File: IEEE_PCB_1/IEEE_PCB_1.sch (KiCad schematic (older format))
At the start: 17 parts, among them U1 555, U2 4017, U3 EG1218, U4 1058TR

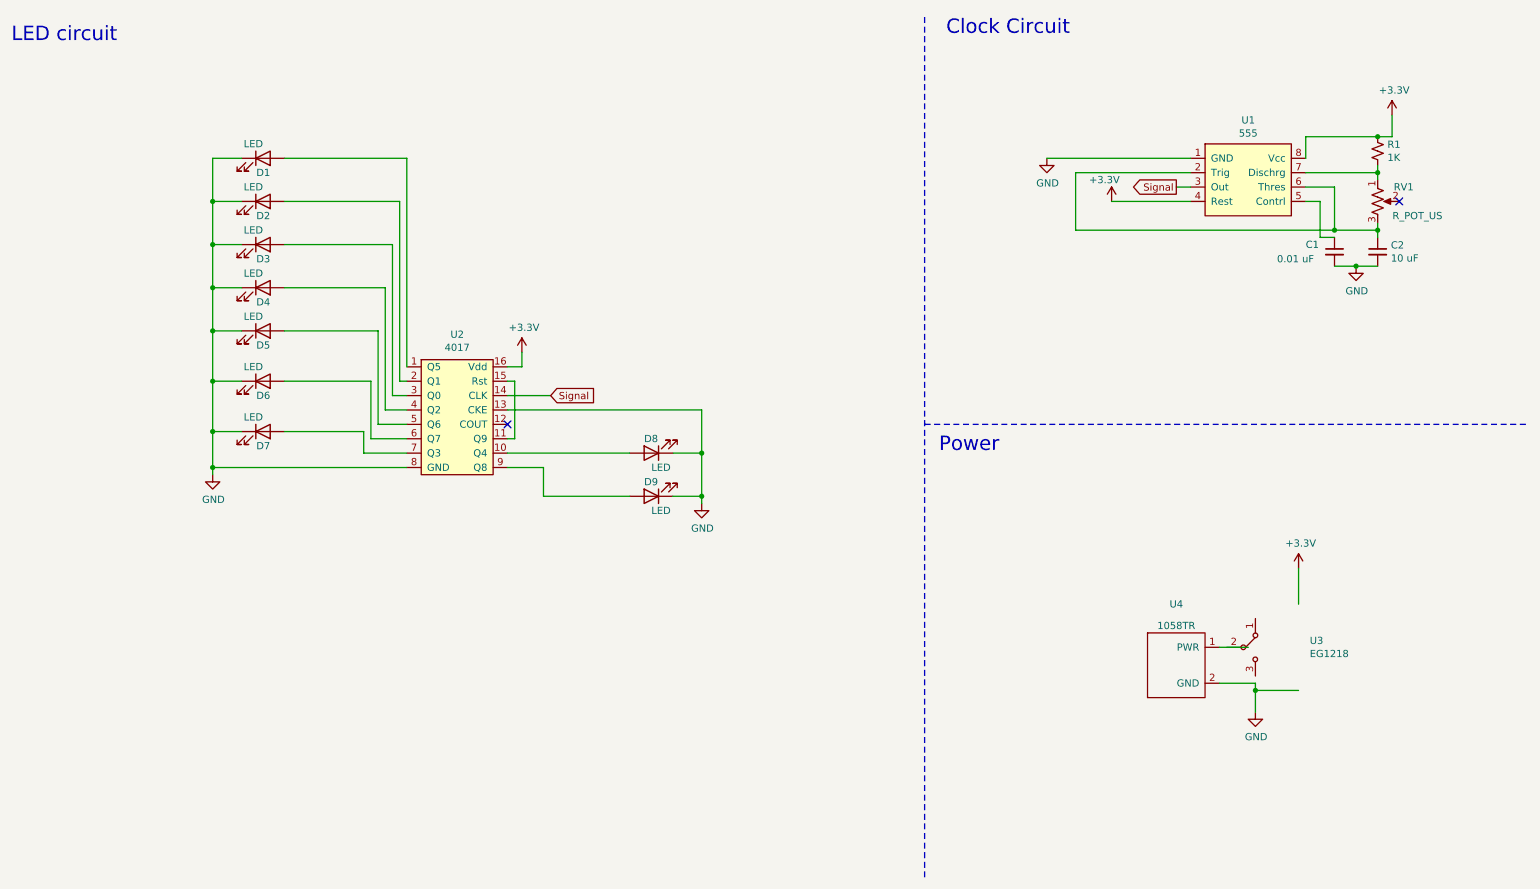
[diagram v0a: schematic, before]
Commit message: Rev4
finished potentiometer footprint
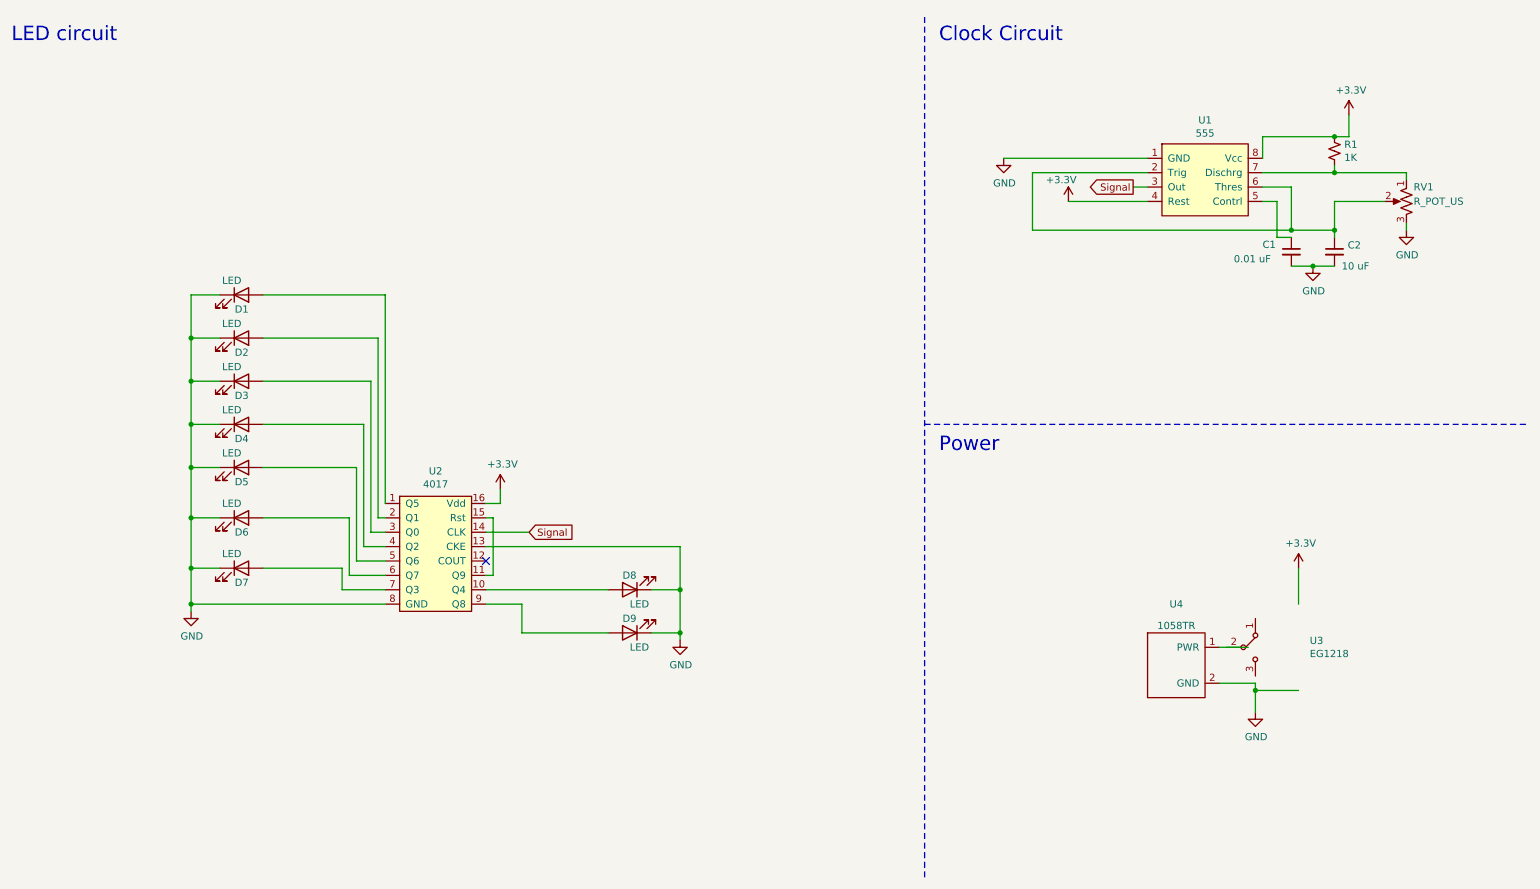
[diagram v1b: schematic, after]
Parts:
- RV1: footprint (none) -> IEEE_PCB_Ornament:CT6EP504
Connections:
- wire segments 81 -> 84
- no-connect marks 2 -> 1
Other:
- moved on the sheet: C1, C2, D1, D2, D3, D4, D5, D6, D7, D8, D9, R1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

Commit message: Rev5
new ball ornament design
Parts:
- removed U4: 1058TR, IEEE_PCB_Ornament:1058TR, symbol IEEE_PCB_Ornament:1058TR
- added U4: CR2025TR, IEEE_PCB_Ornament:CR2025TR, symbol IEEE_PCB_Ornament:CR2025TR
- D1, D2, D3: value LED -> YELLOW
- D4, D5, D6, D7, D8, D9: value LED -> RED
- RV1: value R_POT_US -> 50K
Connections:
- wire segments 84 -> 83
- no-connect marks 1 -> 8
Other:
- moved on the sheet: U2
